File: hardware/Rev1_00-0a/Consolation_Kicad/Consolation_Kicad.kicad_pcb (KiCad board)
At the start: 6 copper layers, 137.5 x 76.6 mm, 434 parts, among them J10 61300311121, J11 5051102291, J12 RPI_CMx_B, J13 5051102291, J14 61300311121, J15 61300311121, J17 61300311121, J18 61300411121, J19 RPI_CMx_A, J2 SJ-3524-SMT-TR, J3 62684-402100ALF, J4 12401598E4#2A, J5 S2B-PH-K-S, J6 2086581001, J7 2998TR, J8 DM3AT-SF-PEJM5, Q1 SSM3K56FS,LF, Q10 SSM3K56FS,LF, Q11 SSM3K56FS,LF, Q14 SSM3K56FS,LF, Q18 SSM3K56FS,LF, Q19 SSM3K56FS,LF, Q20 SSM3K56FS,LF, Q21 SSM3K56FS,LF, Q22 SSM3K56FS,LF, Q23 SSM3K56FS,LF, Q24 SSM3K56FS,LF, Q25 SSM3K56FS,LF, Q26 SSM3K56FS,LF, Q3 SSM3K56FS,LF, Q7 SSM3K56FS,LF, Q8 SSM3K56FS,LF, Q9 SSM3K56FS,LF, U1 BQ25640VDLR, U10 TPS62826DMQR, U11 AP22913W6-7, U15 SN65DSI84ZXHR, U18 AP22913W6-7, U19 SN74LVC1G125DBVR, U2 RP2350A, U21 MCP7940NT-I/MS, U26 TPS61169DCKR, U30 STM6710DWB6F, U31 SN74LVC1G125DBVR, U32 SN74HCS365QPWRQ1, U4 ECS-2016MVQ-120-BP-TR, U5 NAU88C22YG, U6 AP22913W6-7, U7 TPS79901DRVR, U8 GD25Q32CWIGR, U9 TPS61230ARNSR, Y1 12MHz 10pF, Y2 32.768kHz

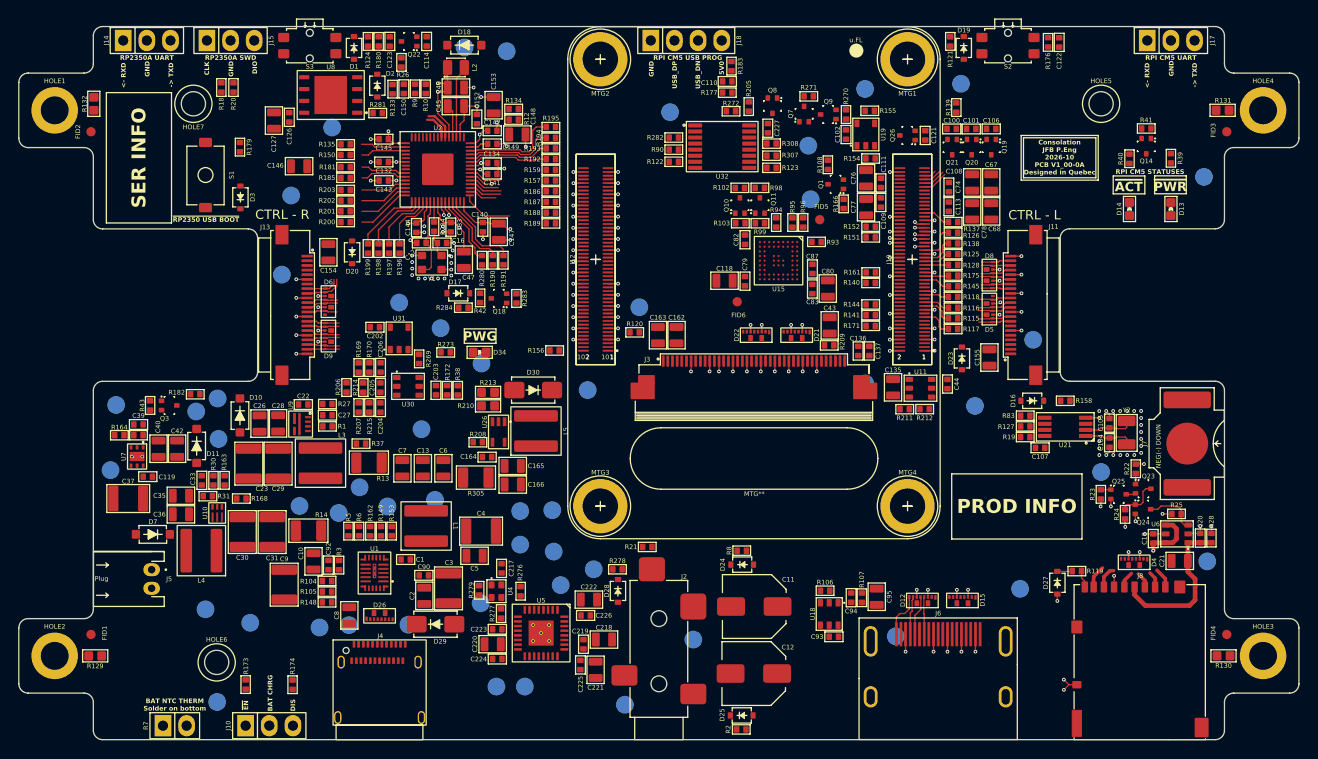
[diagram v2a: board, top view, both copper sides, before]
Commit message: Preliminary routing (DiffPairs, Power planes) in progress Slight changes to schematics to accommodate routing
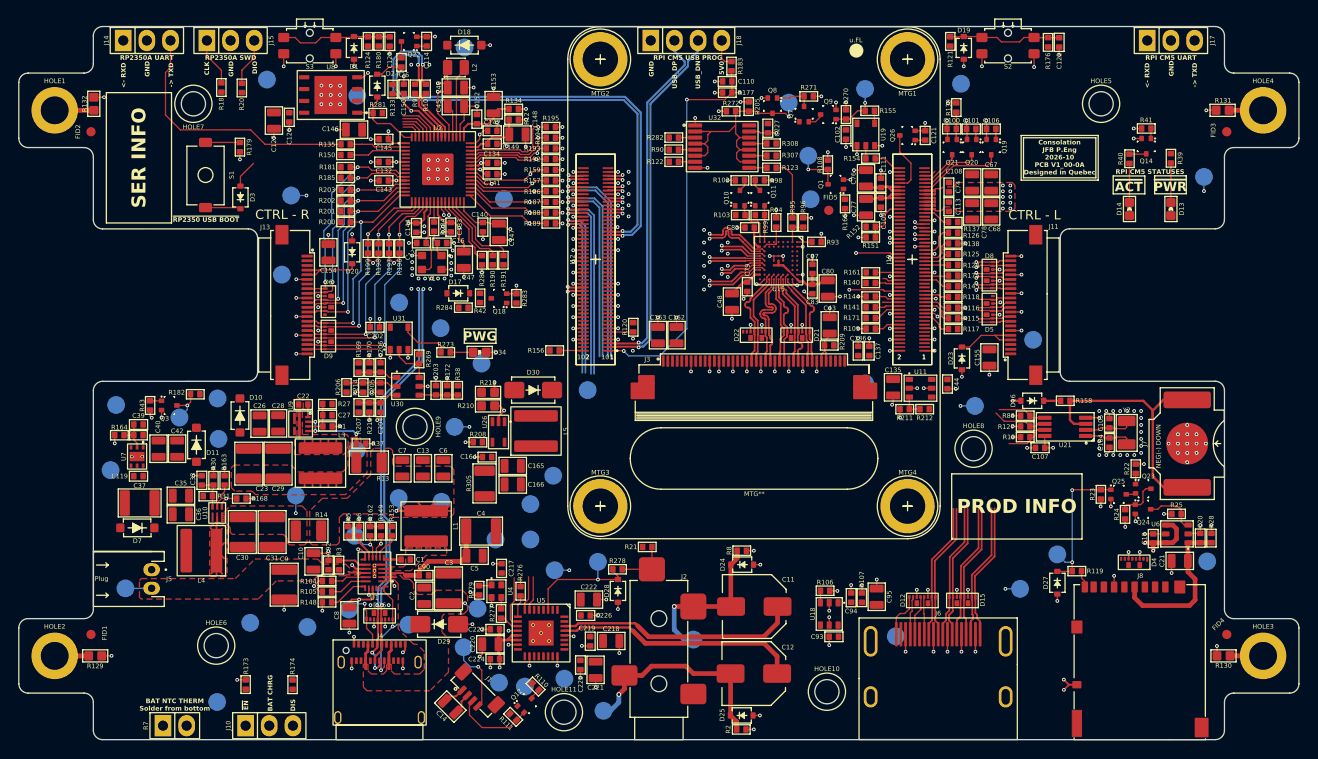
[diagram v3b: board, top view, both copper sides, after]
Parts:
- removed C118: 22u, footprint:CAP_NONPOL_0805
- removed FID6: ~, footprint:FIDUCIAL
- added C14: 22u, footprint:CAP_NONPOL_0805, F.Cu at (86.5, 123.2)
- added C48: 1u, footprint:CAP_NONPOL_0805, F.Cu at (116.7, 79.7)
- added HOLE10: ~, footprint:NPTH_M2, F.Cu at (126.9, 121.5)
- added HOLE11: ~, footprint:NPTH_M2, F.Cu at (98.7, 123.8)
- added HOLE8: ~, footprint:NPTH_M2, F.Cu at (142.7, 95.5)
- added HOLE9: ~, footprint:NPTH_M2, F.Cu at (82.7, 93.1)
- added J1: BM04B-SURS-TF, footprint:BM04B-SURS-TF, F.Cu at (89.2, 121.6)
- added Q12: SSM3K56FS,LF, footprint:SC-75, F.Cu at (94.6, 122.8)
- added R109: 4K7, footprint:RES_0402, F.Cu at (131.6, 82.5)
- added R110: 4K7, footprint:RES_0402, F.Cu at (95.6, 121.0)
- added R111: 4K7, footprint:RES_0402, F.Cu at (93.2, 124.2)
- added TP52: 75 mils, footprint:SMT_TP_75_MILS, B.Cu at (98.7, 120.2)
- added TP53: 75 mils, footprint:SMT_TP_75_MILS, B.Cu at (87.9, 116.8)
- moved TP25 25.9 mm to (66.8, 55.8)
- moved TP23 18.6 mm to (92.2, 68.6)
- moved TP16 12.8 mm to (122.8, 58.3)
- moved TP18 10.0 mm to (151.7, 106.8)
- moved TP38 8.89 mm to (51.5, 110.5)
- moved TP26 8.54 mm to (91.3, 105.2)
- moved C146 7.09 mm to (76.1, 61.2)
- moved TP28 5.20 mm to (97.5, 98.3)
- moved TP35 4.36 mm to (76.5, 57.5)
- moved TP9 3.99 mm to (76.4, 95.6)
- moved TP5 3.56 mm to (86.9, 93.1)
- moved TP41 3.00 mm to (76.2, 104.8)
- moved TP29 2.44 mm to (95.0, 101.4)
- moved TP31 2.39 mm to (102.9, 123.6)
- moved TP6 2.00 mm to (97.7, 108.5)
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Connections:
- C93 pad 2: 5V0_CB -> 5V0
- R122 pad 2: /~{BAT_CHRG_RST} -> /~{CODEC_RST}
- R123 pad 2: /~{RP2350_RST} -> /~{DSI_BRDG_RST}
- R282 pad 2: /~{DSI_BRDG_RST} -> /~{RP2350_RST}
- R307 pad 2: /~{CODEC_RST} -> /~{TFT_RST}
- R90 pad 2: /~{TFT_RST} -> /~{BAT_CHRG_RST}
- U18 pad 4: 5V0_CB -> 5V0
- U18 pad 6: 5V0_CB -> 5V0
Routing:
- net GND: track 133.1 -> 301.5 mm, vias 152 -> 357
- net /CM5_CONN_B/USB_PROG_OTG_ID: track 0.00 -> 67.3 mm, vias 0 -> 4
- net /USB2_DOCK.USB_P: track 0.00 -> 63.7 mm, vias 0 -> 5
- net /USB2_DOCK.USB_N: track 0.00 -> 61.2 mm, vias 0 -> 3
- net /CM5_CONN_B/USB2_RP2350.USB_N: track 0.00 -> 53.0 mm, vias 0 -> 2
- net /CM5_CONN_B/USB2_RP2350.USB_P: track 0.00 -> 53.0 mm, vias 0 -> 2
- net 3V3: track 38.0 -> 90.5 mm, vias 16 -> 51
- net /CM5_CONN_B/DSI1.D3_P: track 0.00 -> 39.5 mm, vias 0 -> 2
- net /CM5_CONN_B/USB_PROG_N: track 0.00 -> 39.2 mm, vias 0 -> 1
- net /CM5_CONN_B/DSI1.D3_N: track 0.00 -> 38.8 mm, vias 0 -> 2
- net /CM5_CONN_B/USB_PROG_P: track 0.00 -> 38.6 mm, vias 0 -> 1
- net /CM5_CONN_B/DSI1.D1_P: track 0.00 -> 37.6 mm, vias 0 -> 2
- net /CM5_CONN_B/DSI1.D1_N: track 0.00 -> 36.9 mm, vias 0 -> 2
- net /CM5_CONN_B/HDMI0.CLK_N: track 0.00 -> 36.5 mm, vias 0 -> 1
- net /CM5_CONN_B/HDMI0.CLK_P: track 0.00 -> 35.9 mm, vias 0 -> 1
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- added copper zone on F.Cu, net /Power Supply/VSYS
- added copper zone on F.Cu, net /TYPE C CHARGER/BAT+
- added copper zone on F.Cu, net 5V0
- added copper zone on F.Cu, net Net-(D29-K)
- added copper zone on F.Cu, net Net-(L1-+)
- added copper zone on F.Cu, net Net-(L3-+)
- added copper zone on F.Cu, net Net-(L3--)
- added copper zone on F.Cu, net Net-(L4-+)
- added copper zone on F.Cu, net Net-(U10-VIN)
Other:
- board text added: "Solder from bottom"
- board text removed: "Solder on bottom"
